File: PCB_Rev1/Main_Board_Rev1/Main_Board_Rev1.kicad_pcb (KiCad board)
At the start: 4 copper layers, 152.4 x 152.4 mm, 83 parts, among them IC1 LT8648SEV#PBF, J1 PRT-14017, J10 B4B-PH-K-S, J11 532610771, J12 532610771, J13 532610771, J2 Conn_01x04_Socket, J3 691137710002, J4 Conn_01x02_Pin, J5 XT60PW-M, J6 Conn_01x02_Pin, J7 Conn_01x02_Pin, J8 Conn_01x02_Pin, J9 B4B-PH-K-S, Q1 AO3400A, Q2 AO3400A, Q3 AO3400A, Q4 IRFHM9331TRPBF, U1 AZ1117IH-3.3TRG1, U2 L298N, X1 B2P-VH, X2 B2P-VH

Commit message: more CP changes
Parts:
- moved TP5 174.3 mm to (166.5, 142.5)
- moved TP4 171.2 mm to (166.5, 135.0)
- moved C8 91.1 mm to (124.0, 138.0), turned to 90 degrees
- moved C9 89.5 mm to (124.5, 132.5), turned to 180 degrees
- moved J7 76.8 mm to (129.5, 147.0)
- moved LED3 71.2 mm to (150.6, 153.6), turned to -90 degrees
- moved LED2 68.2 mm to (150.6, 144.9), turned to 90 degrees
- moved J6 67.6 mm to (134.5, 147.0)
- moved F2 63.5 mm to (145.6, 149.5)
- moved U1 62.1 mm to (131.0, 138.0)
- moved R10 47.4 mm to (145.6, 154.0)
- moved R9 45.5 mm to (145.6, 145.0)
- moved L2 42.3 mm to (111.0, 132.0)
- moved PS1 42.2 mm to (97.2, 133.2)
- moved D1 31.8 mm to (69.5, 140.0), turned to 90 degrees
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
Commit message: more CP commits
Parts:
- moved F2 62.3 mm to (96.6, 111.0)
- moved J6 62.3 mm to (85.5, 108.5)
- moved J7 62.3 mm to (80.5, 108.5)
- moved LED2 62.3 mm to (101.6, 106.4)
- moved LED3 62.3 mm to (101.6, 115.1)
- moved R10 62.3 mm to (96.6, 115.5)
- moved R9 62.3 mm to (96.6, 106.5)
- moved TP4 62.3 mm to (117.5, 96.5)
- moved TP5 62.3 mm to (117.5, 104.0)
- moved F3 60.9 mm to (140.9, 127.1), turned to -90 degrees
- moved J8 60.8 mm to (147.9, 134.1), turned to -90 degrees
- moved C8 58.1 mm to (88.5, 92.0)
- moved C9 58.1 mm to (89.0, 86.5)
- moved U1 58.1 mm to (95.5, 92.0)
- moved R11 55.8 mm to (134.4, 127.0), turned to -90 degrees
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
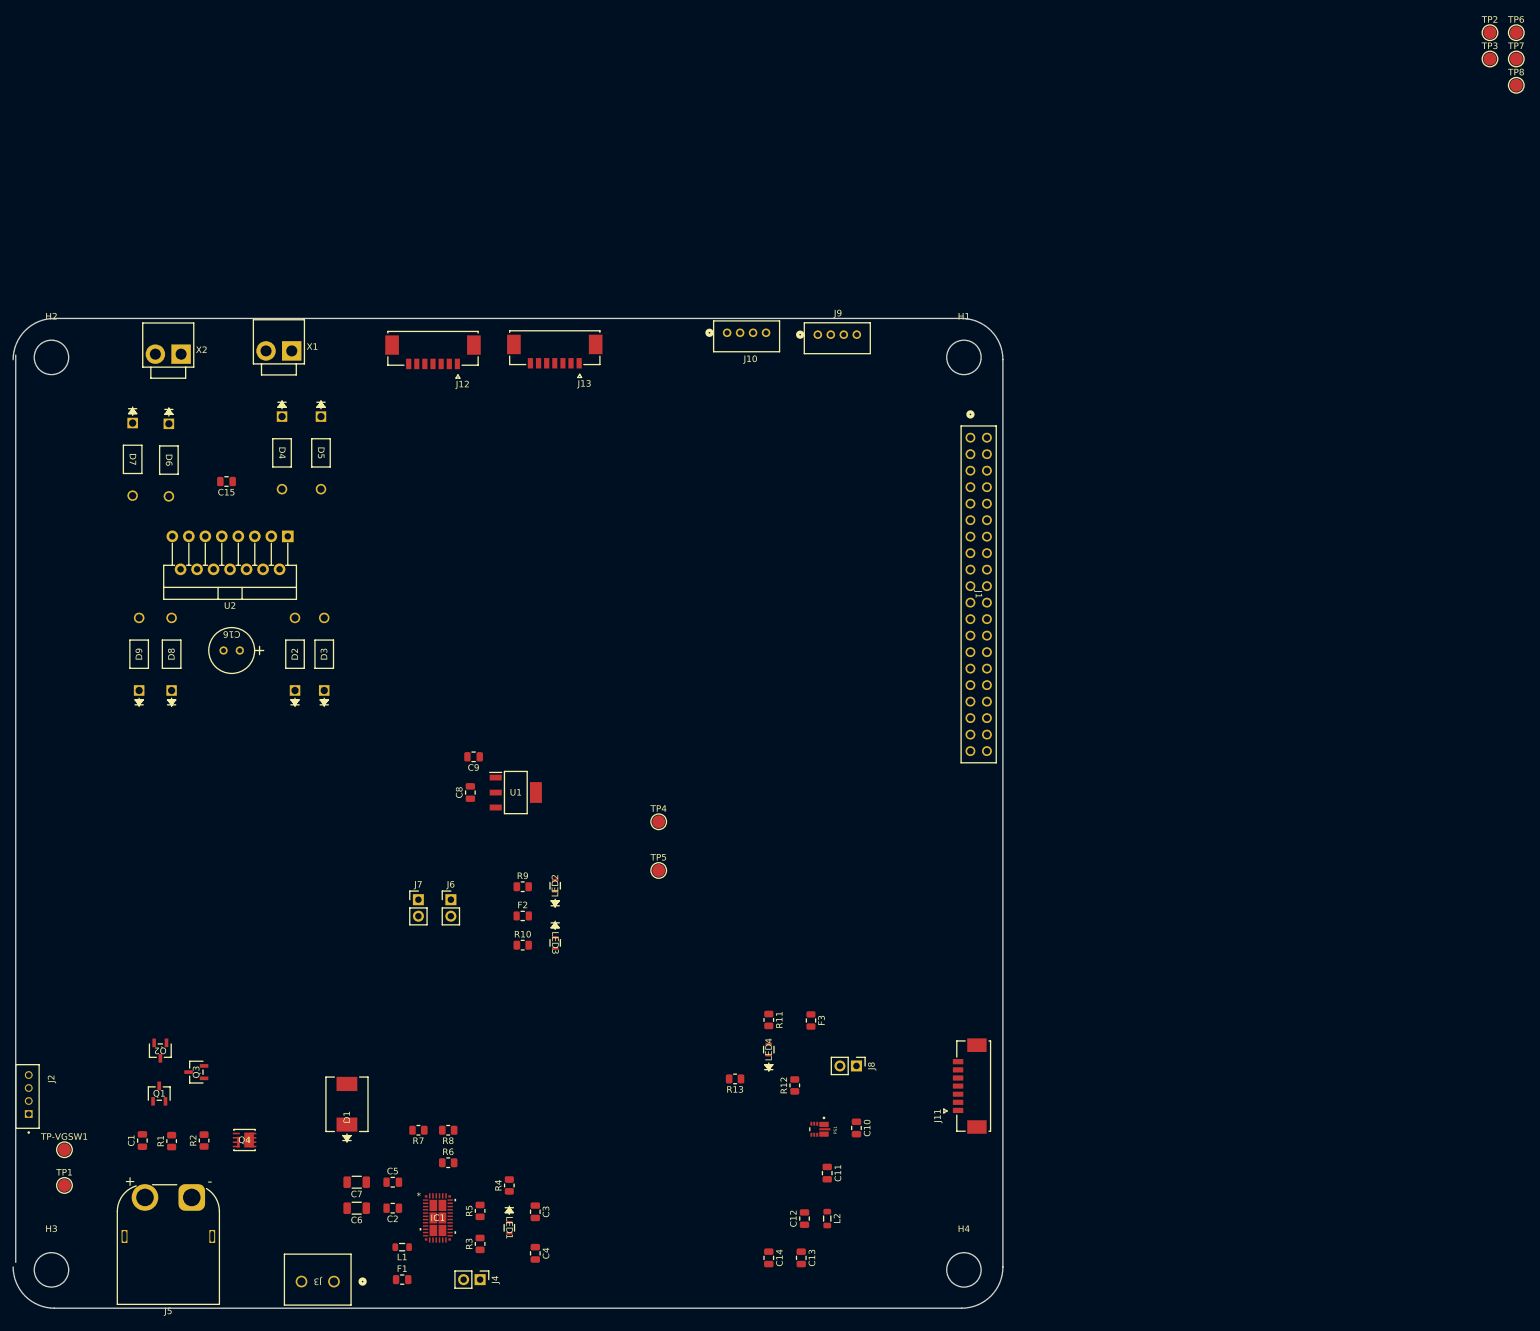
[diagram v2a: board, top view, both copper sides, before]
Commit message: Component Placement complete
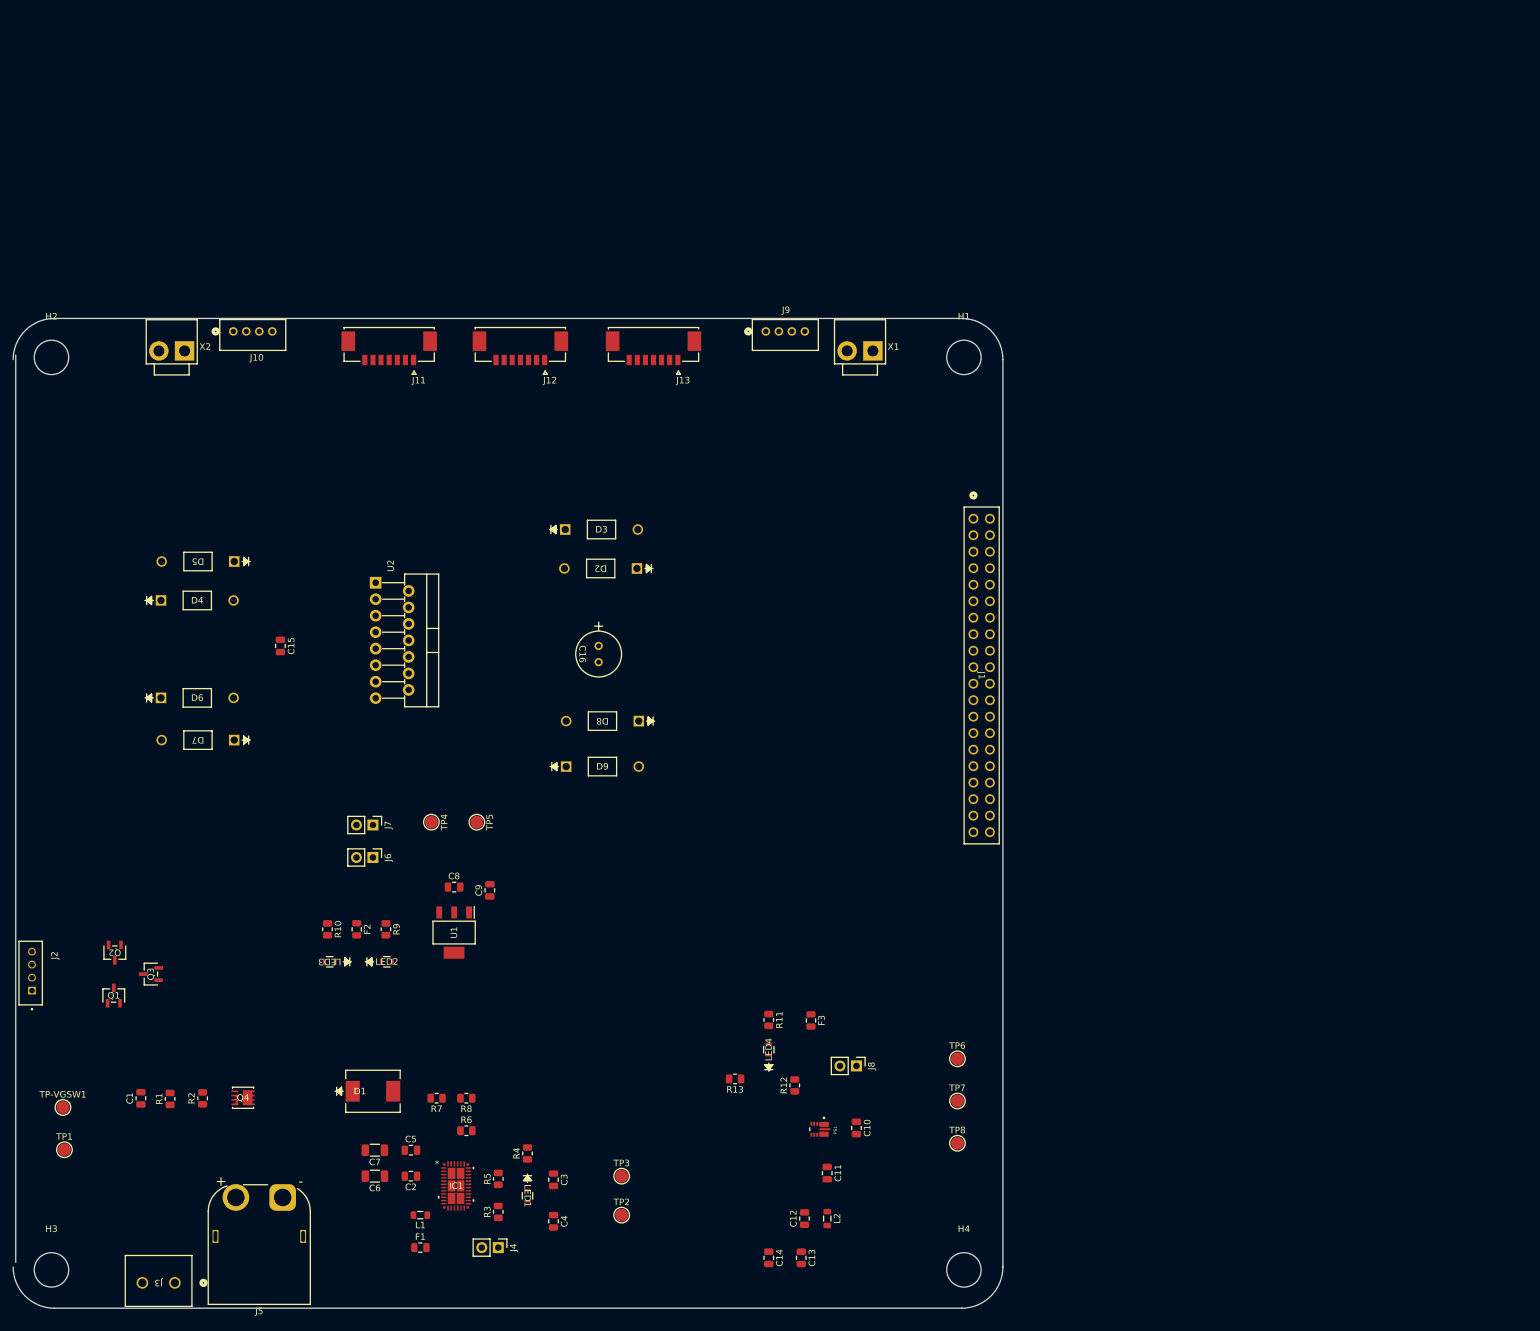
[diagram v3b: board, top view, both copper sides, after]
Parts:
- moved TP2 225.9 mm to (111.8, 157.1)
- moved TP3 217.9 mm to (111.8, 151.1)
- moved TP8 184.2 mm to (163.5, 146.0)
- moved TP7 182.1 mm to (163.5, 139.5)
- moved TP6 179.9 mm to (163.5, 133.0)
- moved J11 145.4 mm to (76.0, 23.0), turned to 180 degrees
- moved X1 89.5 mm to (148.5, 24.0)
- moved J10 76.0 mm to (52.0, 21.0)
- moved D8 72.1 mm to (114.4, 81.0), turned to 180 degrees
- moved D9 66.8 mm to (103.3, 88.0), turned to 0 degrees
- moved D2 55.9 mm to (114.2, 57.5), turned to 180 degrees
- moved C16 55.3 mm to (108.3, 69.4), turned to -90 degrees
- moved D7 51.3 mm to (52.1, 83.9), turned to 180 degrees
- moved D3 44.6 mm to (103.1, 51.5), turned to 0 degrees
- moved D6 42.2 mm to (40.9, 77.4), turned to 0 degrees
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
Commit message: Lidar routing complete
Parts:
- moved D8 1.00 mm to (114.4, 82.0)
- moved D9 0.50 mm to (103.3, 88.5)
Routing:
- net RXD_LIDAR: track 0.00 -> 130.2 mm, vias 0 -> 3
- net TXD_LIDAR: track 0.00 -> 128.4 mm, vias 0 -> 3
- net LIDAR_IO: track 0.00 -> 126.2 mm, vias 0 -> 3
- added copper zone on In2.Cu, net GND
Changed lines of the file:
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@@
 	(footprint "Footprints:Diode_1N4007"
 		(layer "F.Cu")
-		(at 114.431 81 180)
+		(at 114.431 82 180)
 		(tags "1N4007G-T ")
 		(property "Reference" "D8"
@@
 	(footprint "Footprints:Diode_1N4007"
 		(layer "F.Cu")
-		(at 103.255 88)
+		(at 103.255 88.5)
 		(tags "1N4007G-T ")
 		(property "Reference" "D9"
@@
 		(layer "Edge.Cuts")
 	)
+	(segment
+		(start 72.25 45.25)
+		(end 72.25 25.4)
+		(width 0.2)
+		(layer "F.Cu")
+		(net 47)
+	)
+	(segment
+		(start 149 45.5)
+		(end 149 59)
+		(width 0.2)
+		(layer "F.Cu")
+		(net 47)
+	)
+	(segment
+		(start 72.5 45.5)
+		(end 72.25 45.25)
+		(width 0.2)
+		(layer "F.Cu")
+		(net 47)
+	)
+	(via
+		(at 72.5 45.5)
+		(size 0.6)
+		(drill 0.3)
+		(layers "F.Cu" "B.Cu")
+		(net 47)
+	)
+	(via
+		(at 149 45.5)
+		(size 0.6)
+		(drill 0.3)
+		(layers "F.Cu" "B.Cu")
+		(net 47)
+	)
+	(via
+		(at 149 59)
+		(size 0.6)
+		(drill 0.3)
+		(layers "F.Cu" "B.Cu")
+		(net 47)
+	)
+	(segment
+		(start 149.062 58.938)
+		(end 167.438 58.938)
+		(width 0.2)
+		(layer "B.Cu")
+		(net 47)
+	)
+	(segment
+		(start 149 45.5)
+		(end 72.5 45.5)
+		(width 0.2)
+		(layer "B.Cu")
+		(net 47)
+	)
+	(segment
+		(start 149 59)
+		(end 149.062 58.938)
+		(width 0.2)
+		(layer "B.Cu")
+		(net 47)
+	)
+	(segment
+		(start 167.438 58.938)
+		(end 168.5 60)
+		(width 0.2)
+		(layer "B.Cu")
+		(net 47)
+	)
+	(segment
+		(start 148.4 60.965687)
+		(end 148.4 46.5)
+		(width 0.2)
+		(layer "F.Cu")
+		(net 50)
+	)
+	(segment
+		(start 78.5 25.4)
+		(end 78.5 46.5)
+		(width 0.2)
+		(layer "F.Cu")
+		(net 50)
+	)
+	(segment
+		(start 148.434313 61)
+		(end 148.4 60.965687)
+		(width 0.2)
+		(layer "F.Cu")
+		(net 50)
+	)
+	(via
+		(at 78.5 46.5)
+		(size 0.6)
+		(drill 0.3)
+		(layers "F.Cu" "B.Cu")
+		(net 50)
+	)
+	(via
+		(at 148.4 46.5)
+		(size 0.6)
+		(drill 0.3)
+		(layers "F.Cu" "B.Cu")
+		(net 50)
+	)
+	(via
+		(at 148.434313 61)
+		(size 0.6)
+		(drill 0.3)
+		(layers "F.Cu" "B.Cu")
+		(net 50)
+	)
+	(segment
+		(start 78.5 46.5)
+		(end 148.4 46.5)
+		(width 0.2)
+		(layer "B.Cu")
+		(net 50)
+	)
+	(segment
+		(start 167.022 61.062)
+		(end 168.5 62.54)
+		(width 0.2)
+		(layer "B.Cu")
+		(net 50)
+	)
+	(segment
+		(start 148.496313 61.062)
+		(end 167.022 61.062)
+		(width 0.2)
+		(layer "B.Cu")
+		(net 50)
+	)
+	(segment
+		(start 148.434313 61)
+		(end 148.496313 61.062)
+		(width 0.2)
+		(layer "B.Cu")
+		(net 50)
+	)
+	(segment
+		(start 73.5 25.4)
+		(end 73.5 44.5)
+		(width 0.2)
+		(layer "F.Cu")
+		(net 60)
+	)
+	(segment
+		(start 149.5 44.5)
+		(end 149.6 44.6)
+		(width 0.2)
+		(layer "F.Cu")
+		(net 60)
+	)
+	(segment
+		(start 149.6 44.6)
+		(end 149.6 58.338)
+		(width 0.2)
+		(layer "F.Cu")
+		(net 60)
+	)
+	(via
+		(at 73.5 44.5)
+		(size 0.6)
+		(drill 0.3)
+		(layers "F.Cu" "B.Cu")
+		(net 60)
+	)
+	(via
+		(at 149.6 58.338)
+		(size 0.6)
+		(drill 0.3)
+		(layers "F.Cu" "B.Cu")
+		(net 60)
+	)
+	(via
+		(at 149.5 44.5)
+		(size 0.6)
+		(drill 0.3)
+		(layers "F.Cu" "B.Cu")
+		(net 60)
+	)
+	(segment
+		(start 73.5 44.5)
+		(end 149.5 44.5)
+		(width 0.2)
+		(layer "B.Cu")
+		(net 60)
+	)
+	(segment
+		(start 149.6 58.338)
+		(end 149.784 58.522)
+		(width 0.2)
+		(layer "B.Cu")
+		(net 60)
+	)
+	(segment
+		(start 167.438 58.522)
+		(end 168.5 57.46)
+		(width 0.2)
+		(layer "B.Cu")
+		(net 60)
+	)
+	(segment
+		(start 149.784 58.522)
+		(end 167.438 58.522)
+		(width 0.2)
+		(layer "B.Cu")
+		(net 60)
+	)
+	(zone
+		(net 2)
+		(net_name "GND")
+		(layer "In2.Cu")
+		(name "GND")
+		(hatch edge 0.5)
+		(connect_pads
+			(clearance 0.5)
+		)
+		(min_thickness 0.25)
+		(filled_areas_thickness no)
+		(fill yes
+			(thermal_gap 0.5)
+			(thermal_bridge_width 0.5)
+		)
+		(polygon
+			(pts
+				(xy 14.190237 14.520122) (xy 175.690237 14.520122) (xy 173.690237 182.520122) (xy 13.190237 180.520122)
+			)
+		)
+	)
 )

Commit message: routing attempt
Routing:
- net GPIO13: track 0.00 -> 144.2 mm, vias 0 -> 4
- net GPIO12: track 0.00 -> 127.5 mm, vias 0 -> 5
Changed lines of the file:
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@@
 		)
 		(property "Footprint" "Footprints:Diode_1N4007"
-			(at 0 0 360)
+			(at 0 0 0)
 			(layer "F.Fab")
 			(hide yes)
@@
 		)
 		(property "Datasheet" ""
-			(at 0 0 360)
+			(at 0 0 0)
 			(layer "F.Fab")
 			(hide yes)
@@
 		)
 		(property "Description" "Diode"
-			(at 0 0 360)
+			(at 0 0 0)
 			(layer "F.Fab")
 			(hide yes)
@@
 		)
 		(property "Footprint" "Footprints:Diode_1N4007"
-			(at 0 0 360)
+			(at 0 0 0)
 			(layer "F.Fab")
 			(hide yes)
@@
 		)
 		(property "Datasheet" ""
-			(at 0 0 360)
+			(at 0 0 0)
 			(layer "F.Fab")
 			(hide yes)
@@
 		)
 		(property "Description" "Diode"
-			(at 0 0 360)
+			(at 0 0 0)
 			(layer "F.Fab")
 			(hide yes)
@@
 		(at 76 23 180)
 		(property "Reference" "J11"
-			(at -4.575 -5.543 360)
+			(at -4.575 -5.543 0)
 			(layer "F.SilkS")
 			(effects
@@
 		)
 		(property "Value" "532610771"
-			(at 1.775 4.965 360)
+			(at 1.775 4.965 0)
 			(layer "F.Fab")
 			(effects
@@
 		)
 		(property "Footprint" "Footprints:MOLEX_connector"
-			(at 0 0 360)
+			(at 0 0 0)
 			(layer "F.Fab")
 			(hide yes)
@@
 		)
 		(property "Datasheet" ""
-			(at 0 0 360)
+			(at 0 0 0)
 			(layer "F.Fab")
 			(hide yes)
@@
 		)
 		(property "Description" "\nPicoblade Connector, 7 Circuit Single Row, Right Angle Surface Mount SMT PCB\n"
-			(at 0 0 360)
+			(at 0 0 0)
 			(layer "F.Fab")
 			(hide yes)
@@
 		)
 		(property "Footprint" "Footprints:Diode_1N4007"
-			(at 0 0 360)
+			(at 0 0 0)
 			(layer "F.Fab")
 			(hide yes)
@@
 		)
 		(property "Datasheet" ""
-			(at 0 0 360)
+			(at 0 0 0)
 			(layer "F.Fab")
 			(hide yes)
@@
 		)
 		(property "Description" "Diode"
-			(at 0 0 360)
+			(at 0 0 0)
 			(layer "F.Fab")
 			(hide yes)
@@
 		)
 		(property "Footprint" "Footprints:D1_Bi-dir"
-			(at 0 0 360)
+			(at 0 0 0)
 			(layer "F.Fab")
 			(hide yes)
@@
 		)
 		(property "Datasheet" ""
-			(at 0 0 360)
+			(at 0 0 0)
 			(layer "F.Fab")
 			(hide yes)
@@
 		)
 		(property "Description" ""
-			(at 0 0 360)
+			(at 0 0 0)
 			(layer "F.Fab")
 			(hide yes)
@@
 		)
 		(property "Footprint" "Footprints:LED_0VS75000_WRE"
-			(at 0 0 360)
+			(at 0 0 0)
 			(layer "F.Fab")
 			(hide yes)
@@
 		)
 		(property "Datasheet" "150080VS75000"
-			(at 0 0 360)
+			(at 0 0 0)
 			(layer "F.Fab")
 			(hide yes)
@@
 		)
 		(property "Description" ""
-			(at 0 0 360)
+			(at 0 0 0)
 			(layer "F.Fab")
 			(hide yes)
@@
 		(tags "capacitor")
 		(property "Reference" "C8"
-			(at 0 -1.68 360)
+			(at 0 -1.68 0)
 			(layer "F.SilkS")
 			(effects
@@
 		)
 		(property "Value" "10uF"
-			(at 0 1.68 360)
+			(at 0 1.68 0)
 			(layer "F.Fab")
 			(effects
@@
 		)
 		(fp_text user "${REFERENCE}"
-			(at 0 0 360)
+			(at 0 0 0)
 			(layer "F.Fab")
 			(effects
@@
 		)
 		(property "Footprint" "Footprints:Diode_1N4007"
-			(at 0 0 360)
+			(at 0 0 0)
 			(layer "F.Fab")
 			(hide yes)
@@
 		)
 		(property "Datasheet" ""
-			(at 0 0 360)
+			(at 0 0 0)
 			(layer "F.Fab")
 			(hide yes)
@@
 		)
 		(property "Description" "Diode"
-			(at 0 0 360)
+			(at 0 0 0)
 			(layer "F.Fab")
 			(hide yes)
@@
 		)
 		(fp_text user "${REFERENCE}"
-			(at 0 1.27 360)
+			(at 0 1.27 0)
 			(layer "F.Fab")
 			(effects
@@
 		)
 		(property "Footprint" "Footprints:Diode_1N4007"
-			(at 0 0 360)
+			(at 0 0 0)
 			(layer "F.Fab")
 			(hide yes)
@@
 		)
 		(property "Datasheet" ""
-			(at 0 0 360)
+			(at 0 0 0)
 			(layer "F.Fab")
 			(hide yes)
@@
 		)
 		(property "Description" "Diode"
-			(at 0 0 360)
+			(at 0 0 0)
 			(layer "F.Fab")
 			(hide yes)
@@
 		)
 		(property "Footprint" "Footprints:LED_0VS75000_WRE"
-			(at 0 0 360)
+			(at 0 0 0)
 			(layer "F.Fab")
 			(hide yes)
@@
 		)
 		(property "Datasheet" "150080VS75000"
-			(at 0 0 360)
+			(at 0 0 0)
 			(layer "F.Fab")
 			(hide yes)
@@
 		)
 		(property "Description" ""
-			(at 0 0 360)
+			(at 0 0 0)
 			(layer "F.Fab")
 			(hide yes)
@@
 		)
 		(property "Footprint" "Footprints:Diode_1N4007"
-			(at 0 0 360)
+			(at 0 0 0)
 			(layer "F.Fab")
 			(hide yes)
@@
 		)
 		(property "Datasheet" ""
-			(at 0 0 360)
+			(at 0 0 0)
 			(layer "F.Fab")
 			(hide yes)
@@
 		)
 		(property "Description" "Diode"
-			(at 0 0 360)
+			(at 0 0 0)
 			(layer "F.Fab")
 			(hide yes)
@@
 		)
 		(property "Footprint" "Footprints:Diode_1N4007"
-			(at 0 0 360)
+			(at 0 0 0)
 			(layer "F.Fab")
 			(hide yes)
@@
 		)
 		(property "Datasheet" ""
-			(at 0 0 360)
+			(at 0 0 0)
 			(layer "F.Fab")
 			(hide yes)
@@
 		)
 		(property "Description" "Diode"
-			(at 0 0 360)
+			(at 0 0 0)
 			(layer "F.Fab")
 			(hide yes)
@@
 		)
 		(property "Footprint" "Footprints:Diode_1N4007"
-			(at 0 0 360)
+			(at 0 0 0)
 			(layer "F.Fab")
 			(hide yes)
@@
 		)
 		(property "Datasheet" ""
-			(at 0 0 360)
+			(at 0 0 0)
 			(layer "F.Fab")
 			(hide yes)
@@
 		)
 		(property "Description" "Diode"
-			(at 0 0 360)
+			(at 0 0 0)
 			(layer "F.Fab")
 			(hide yes)
@@
 		)
 		(fp_text user "${REFERENCE}"
-			(at 0 1.27 360)
+			(at 0 1.27 0)
 			(layer "F.Fab")
 			(effects
@@
 		(net 60)
 	)
+	(segment
+		(start 93.7 25.4)
+		(end 93.7 84.7)
+		(width 0.2)
+		(layer "F.Cu")
+		(net 61)
+	)
+	(segment
+		(start 149.4 72.6)
+		(end 149.4 84.885421)
+		(width 0.2)
+		(layer "F.Cu")
+		(net 61)
+	)
+	(via
+		(at 149.4 84.885421)
+		(size 0.6)
+		(drill 0.3)
+		(layers "F.Cu" "B.Cu")
+		(net 61)
+	)
+	(via
+		(at 93.7 84.7)
+		(size 0.6)
+		(drill 0.3)
+		(layers "F.Cu" "B.Cu")
+		(net 61)
+	)
+	(via
+		(at 149.5 72.5)
+		(size 0.6)
+		(drill 0.3)
+		(layers "F.Cu" "B.Cu")
+		(net 61)
+	)
+	(via
+		(at 93.7 84.7)
+		(size 0.6)
+		(drill 0.3)
+		(layers "F.Cu" "B.Cu")
+		(net 61)
+	)
+	(via
+		(at 149.4 84.885421)
+		(size 0.6)
+		(drill 0.3)
+		(layers "F.Cu" "B.Cu")
+		(net 61)
+	)
+	(segment
+		(start 149.214579 84.7)
+		(end 93.7 84.7)
+		(width 0.2)
+		(layer "B.Cu")
+		(net 61)
+	)
+	(segment
+		(start 149.4 84.885421)
+		(end 149.214579 84.7)
+		(width 0.2)
+		(layer "B.Cu")
+		(net 61)
+	)
+	(segment
+		(start 149.5 72.5)
+		(end 149.4 72.6)
+		(width 0.2)
+		(layer "B.Cu")
+		(net 61)
+	)
+	(segment
+		(start 150 75)
+		(end 150 85.5)
+		(width 0.2)
+		(layer "F.Cu")
+		(net 75)
+	)
+	(segment
+		(start 92.45 25.4)
+		(end 92.45 85.45)
+		(width 0.2)
+		(layer "F.Cu")
+		(net 75)
+	)
+	(segment
+		(start 92.45 85.45)
+		(end 92.5 85.5)
+		(width 0.2)
+		(layer "F.Cu")
+		(net 75)
+	)
+	(via
+		(at 150 85.5)
+		(size 0.6)
+		(drill 0.3)
+		(layers "F.Cu" "B.Cu")
+		(net 75)
+	)
+	(via
+		(at 150 75)
+		(size 0.6)
+		(drill 0.3)
+		(layers "F.Cu" "B.Cu")
+		(net 75)
+	)
+	(via
+		(at 92.5 85.5)
+		(size 0.6)
+		(drill 0.3)
+		(layers "F.Cu" "B.Cu")
+		(net 75)
+	)
+	(via
+		(at 163 75)
+		(size 0.6)
+		(drill 0.3)
+		(layers "F.Cu" "B.Cu")
+		(net 75)
+	)
+	(segment
+		(start 150 75)
+		(end 163 75)
+		(width 0.2)
+		(layer "B.Cu")
+		(net 75)
+	)
+	(segment
+		(start 164 75)
+		(end 165.72 75)
+		(width 0.2)
+		(layer "B.Cu")
+		(net 75)
+	)
+	(segment
+		(start 150 85.5)
+		(end 92.5 85.5)
+		(width 0.2)
+		(layer "B.Cu")
+		(net 75)
+	)
+	(segment
+		(start 165.72 75)
+		(end 165.96 75.24)
+		(width 0.2)
+		(layer "B.Cu")
+		(net 75)
+	)
+	(segment
+		(start 163 75)
+		(end 164 75)
+		(width 0.2)
+		(layer "B.Cu")
+		(net 75)
+	)
 	(zone
